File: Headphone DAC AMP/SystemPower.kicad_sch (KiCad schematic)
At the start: 11 parts, among them U6 MCP1727-1802xSN, U7 MCP1727-3302xSN, U9 TPS717XX

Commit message: Swapped to 0603 caps in order to compact design
Planning on a 100x70mm board shape
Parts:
- C44, C45, C46, C47, C48, C49, C61, C62: footprint Capacitor_SMD:C_0805_2012Metric_Pad1.18x1.45mm_HandSolder -> Capacitor_SMD:C_0603_1608Metric_Pad1.08x0.95mm_HandSolder
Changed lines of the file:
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@@
 			)
 		)
-		(property "Footprint" "Capacitor_SMD:C_0805_2012Metric_Pad1.18x1.45mm_HandSolder"
+		(property "Footprint" "Capacitor_SMD:C_0603_1608Metric_Pad1.08x0.95mm_HandSolder"
 			(at 47.9552 41.91 0)
 			(effects
@@
 			)
 		)
-		(property "Footprint" "Capacitor_SMD:C_0805_2012Metric_Pad1.18x1.45mm_HandSolder"
+		(property "Footprint" "Capacitor_SMD:C_0603_1608Metric_Pad1.08x0.95mm_HandSolder"
 			(at 100.0252 39.37 0)
 			(effects
@@
 			)
 		)
-		(property "Footprint" "Capacitor_SMD:C_0805_2012Metric_Pad1.18x1.45mm_HandSolder"
+		(property "Footprint" "Capacitor_SMD:C_0603_1608Metric_Pad1.08x0.95mm_HandSolder"
 			(at 36.5252 41.91 0)
 			(effects
@@
 			)
 		)
-		(property "Footprint" "Capacitor_SMD:C_0805_2012Metric_Pad1.18x1.45mm_HandSolder"
+		(property "Footprint" "Capacitor_SMD:C_0603_1608Metric_Pad1.08x0.95mm_HandSolder"
 			(at 103.8352 104.14 0)
 			(effects
@@
 			)
 		)
-		(property "Footprint" "Capacitor_SMD:C_0805_2012Metric_Pad1.18x1.45mm_HandSolder"
+		(property "Footprint" "Capacitor_SMD:C_0603_1608Metric_Pad1.08x0.95mm_HandSolder"
 			(at 105.1052 160.02 0)
 			(effects
@@
 			)
 		)
-		(property "Footprint" "Capacitor_SMD:C_0805_2012Metric_Pad1.18x1.45mm_HandSolder"
+		(property "Footprint" "Capacitor_SMD:C_0603_1608Metric_Pad1.08x0.95mm_HandSolder"
 			(at 40.3352 106.68 0)
 			(effects
@@
 			)
 		)
-		(property "Footprint" "Capacitor_SMD:C_0805_2012Metric_Pad1.18x1.45mm_HandSolder"
+		(property "Footprint" "Capacitor_SMD:C_0603_1608Metric_Pad1.08x0.95mm_HandSolder"
 			(at 51.7652 106.68 0)
 			(effects
@@
 			)
 		)
-		(property "Footprint" "Capacitor_SMD:C_0805_2012Metric_Pad1.18x1.45mm_HandSolder"
+		(property "Footprint" "Capacitor_SMD:C_0603_1608Metric_Pad1.08x0.95mm_HandSolder"
 			(at 41.6052 161.29 0)
 			(effects

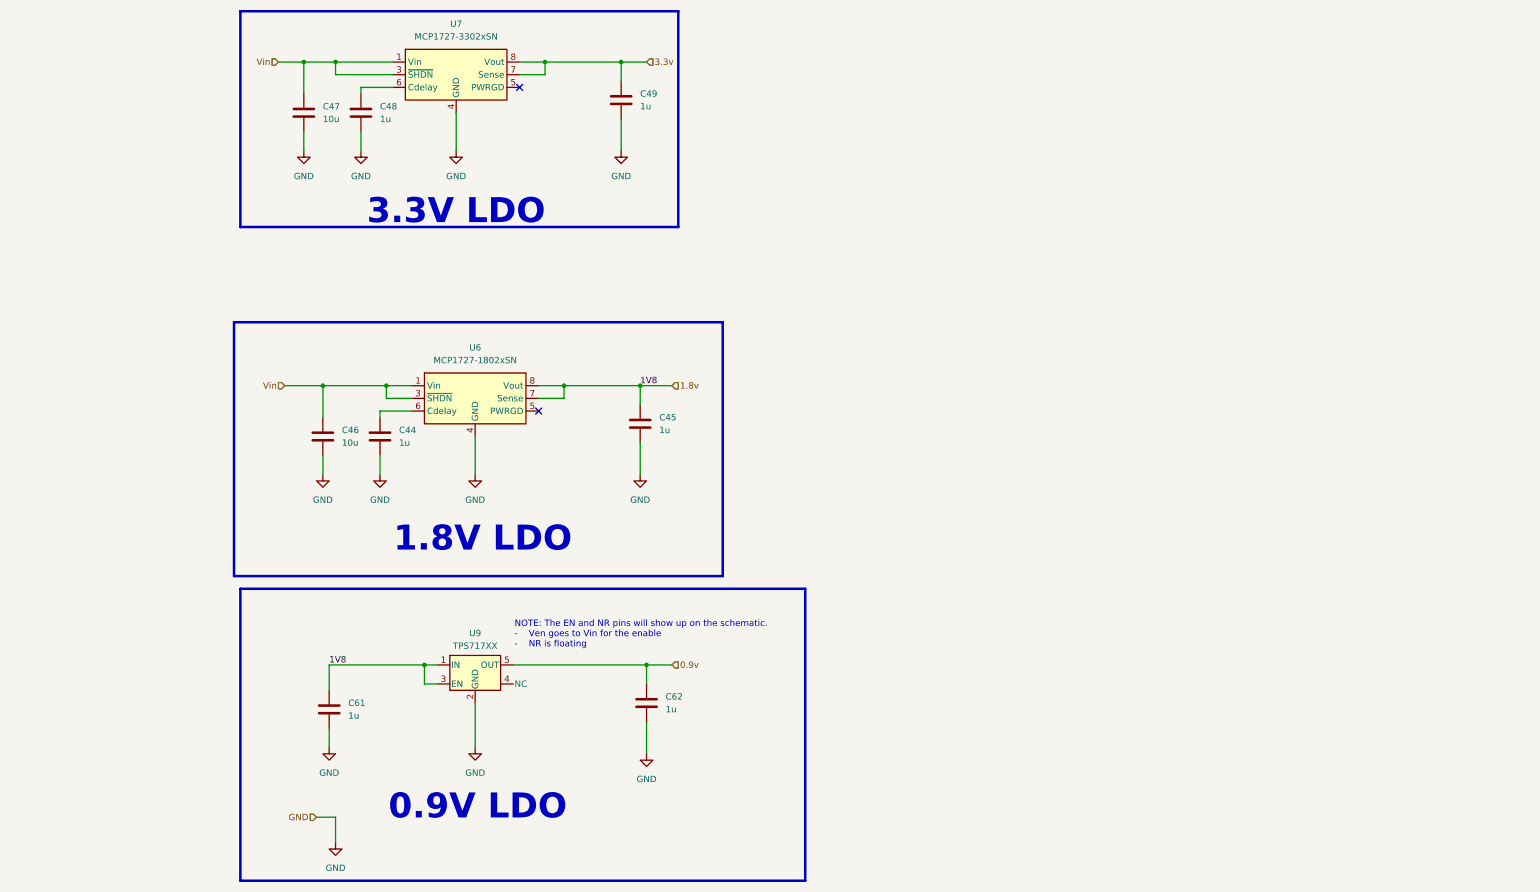
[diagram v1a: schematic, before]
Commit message: (Post Board Order) updated BOM with component links
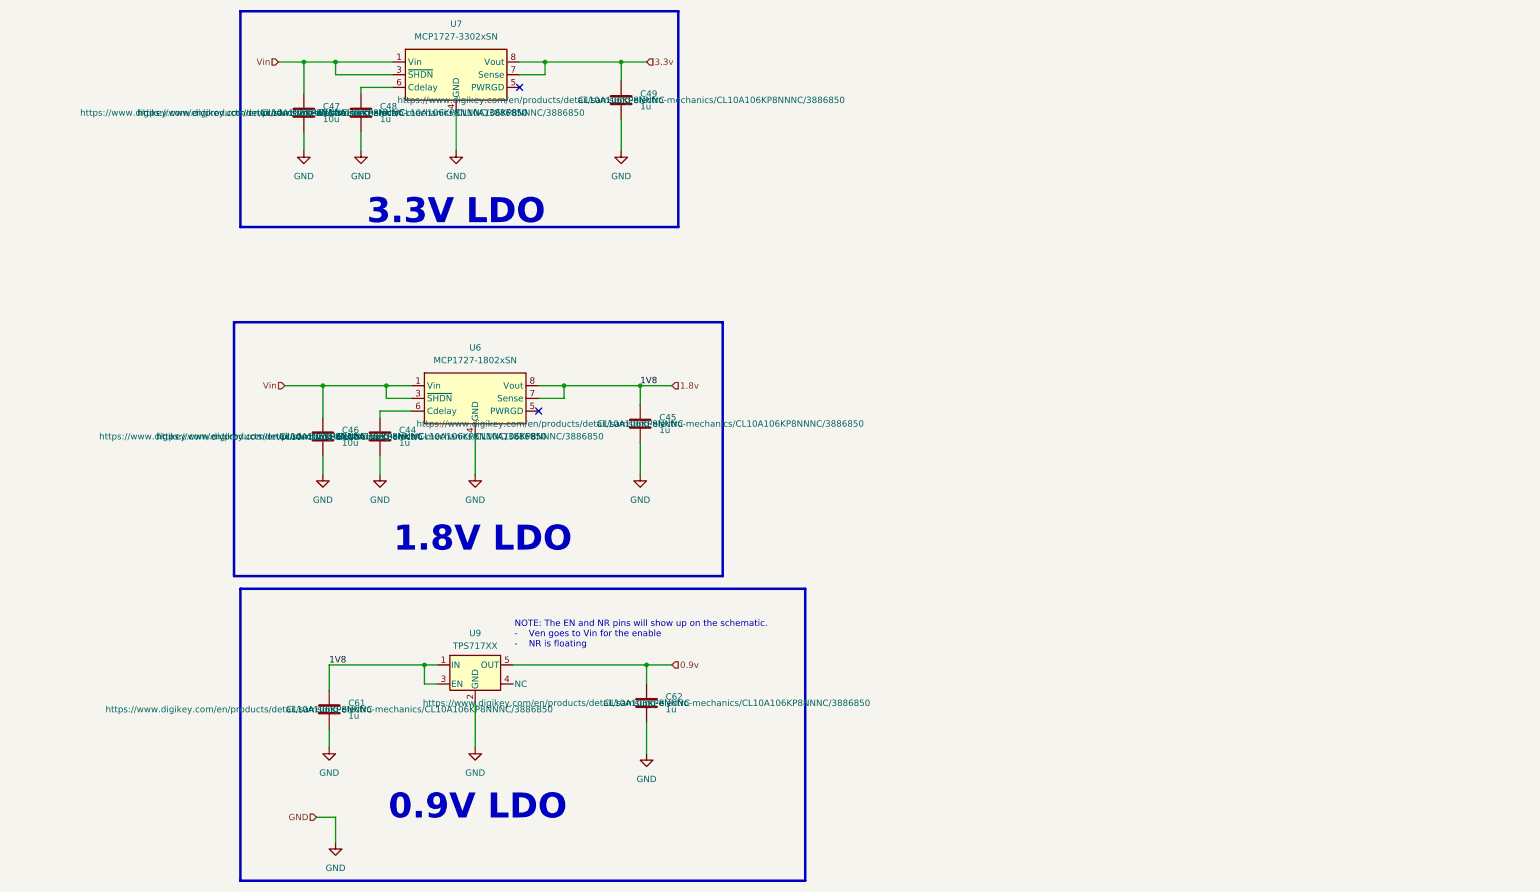
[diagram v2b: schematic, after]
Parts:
- C44, C45, C46, C47, C48, C49, C61, C62: CUI_PURCHASE_URL (none) -> https://www.digikey.com/en/products/detail/samsung-electro-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; Mouser Part Number (none) -> CL10A106KP8NNNC
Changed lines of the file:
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@@
+			)
+		)
+		(property "CUI_PURCHASE_URL" "https://www.digikey.com/en/products/detail/samsung-electro-mechanics/CL10A106KP8NNNC/3886850"
+			(at 46.99 38.1 0)
+			(effects
+				(font
+					(size 1.27 1.27)
+				)
+			)
+		)
+		(property "Mouser Part Number" "CL10A106KP8NNNC"
+			(at 46.99 38.1 0)
+			(effects
+				(font
+					(size 1.27 1.27)
+				)
 			)
 		)
@@
 			)
 		)
+		(property "CUI_PURCHASE_URL" "https://www.digikey.com/en/products/detail/samsung-electro-mechanics/CL10A106KP8NNNC/3886850"
+			(at 99.06 35.56 0)
+			(effects
+				(font
+					(size 1.27 1.27)
+				)
+			)
+		)
+		(property "Mouser Part Number" "CL10A106KP8NNNC"
+			(at 99.06 35.56 0)
+			(effects
+				(font
+					(size 1.27 1.27)
+				)
+			)
+		)
 		(pin "2"
 		)
@@
 			)
 		)
+		(property "CUI_PURCHASE_URL" "https://www.digikey.com/en/products/detail/samsung-electro-mechanics/CL10A106KP8NNNC/3886850"
+			(at 35.56 38.1 0)
+			(effects
+				(font
+					(size 1.27 1.27)
+				)
+			)
+		)
+		(property "Mouser Part Number" "CL10A106KP8NNNC"
+			(at 35.56 38.1 0)
+			(effects
+				(font
+					(size 1.27 1.27)
+				)
+			)
+		)
 		(pin "2"
 		)
@@
 			)
 		)
+		(property "CUI_PURCHASE_URL" "https://www.digikey.com/en/products/detail/samsung-electro-mechanics/CL10A106KP8NNNC/3886850"
+			(at 102.87 100.33 0)
+			(effects
+				(font
+					(size 1.27 1.27)
+				)
+			)
+		)
+		(property "Mouser Part Number" "CL10A106KP8NNNC"
+			(at 102.87 100.33 0)
+			(effects
+				(font
+					(size 1.27 1.27)
+				)
+			)
+		)
 		(pin "2"
 		)
@@
 			)
 		)
+		(property "CUI_PURCHASE_URL" "https://www.digikey.com/en/products/detail/samsung-electro-mechanics/CL10A106KP8NNNC/3886850"
+			(at 104.14 156.21 0)
+			(effects
+				(font
+					(size 1.27 1.27)
+				)
+			)
+		)
+		(property "Mouser Part Number" "CL10A106KP8NNNC"
+			(at 104.14 156.21 0)
+			(effects
+				(font
+					(size 1.27 1.27)
+				)
+			)
+		)
 		(pin "2"
 		)
@@
 			)
 		)
+		(property "CUI_PURCHASE_URL" "https://www.digikey.com/en/products/detail/samsung-electro-mechanics/CL10A106KP8NNNC/3886850"
+			(at 39.37 102.87 0)
+			(effects
+				(font
+					(size 1.27 1.27)
+				)
+			)
+		)
+		(property "Mouser Part Number" "CL10A106KP8NNNC"
+			(at 39.37 102.87 0)
+			(effects
+				(font
+					(size 1.27 1.27)
+				)
+			)
+		)
 		(pin "2"
 		)
@@
 			)
 		)
+		(property "CUI_PURCHASE_URL" "https://www.digikey.com/en/products/detail/samsung-electro-mechanics/CL10A106KP8NNNC/3886850"
+			(at 50.8 102.87 0)
+			(effects
+				(font
+					(size 1.27 1.27)
+				)
+			)
+		)
+		(property "Mouser Part Number" "CL10A106KP8NNNC"
+			(at 50.8 102.87 0)
+			(effects
+				(font
+					(size 1.27 1.27)
+				)
+			)
+		)
 		(pin "1"
 		)
@@
 			)
 		)
+		(property "CUI_PURCHASE_URL" "https://www.digikey.com/en/products/detail/samsung-electro-mechanics/CL10A106KP8NNNC/3886850"
+			(at 40.64 157.48 0)
+			(effects
+				(font
+					(size 1.27 1.27)
+				)
+			)
+		)
+		(property "Mouser Part Number" "CL10A106KP8NNNC"
+			(at 40.64 157.48 0)
+			(effects
+				(font
+					(size 1.27 1.27)
+				)
+			)
+		)

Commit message: Removed DAC Components
Removed all analog components and increased vias to 0.3mm
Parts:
- U9: footprint Package_TO_SOT_SMD:SOT-353_SC-70-5 -> Package_TO_SOT_SMD:SOT-23-5

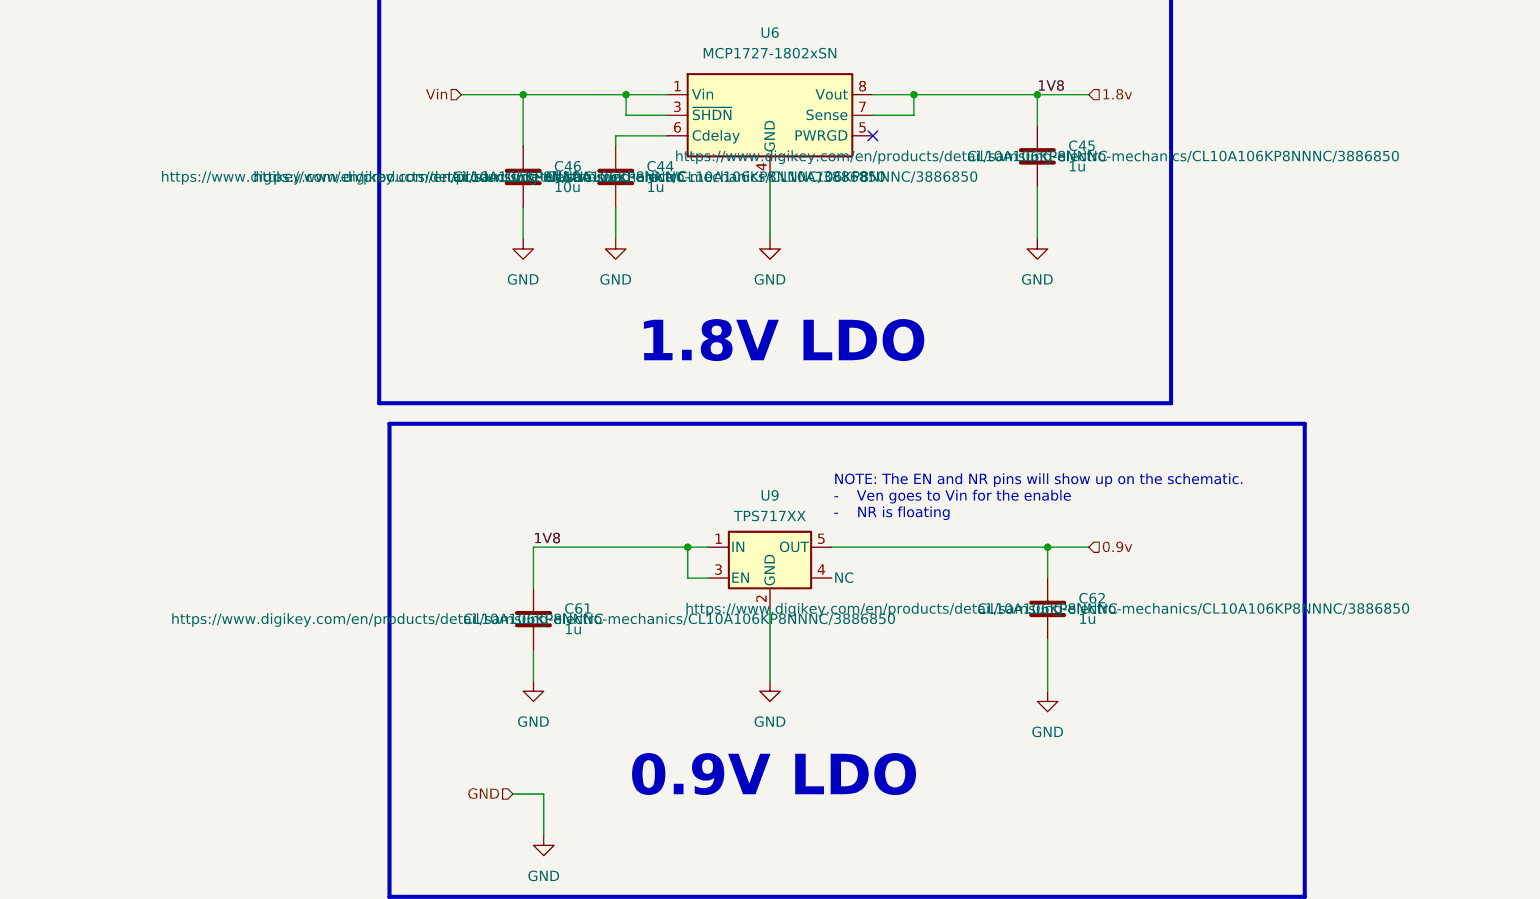
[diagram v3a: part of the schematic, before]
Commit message: Update capacitor footprints
Changed several capacitor footprints in schematic files from 0402/hand-solder variants to standard 0603_1608Metric. Updated PCB with new net and additional property fields for components.
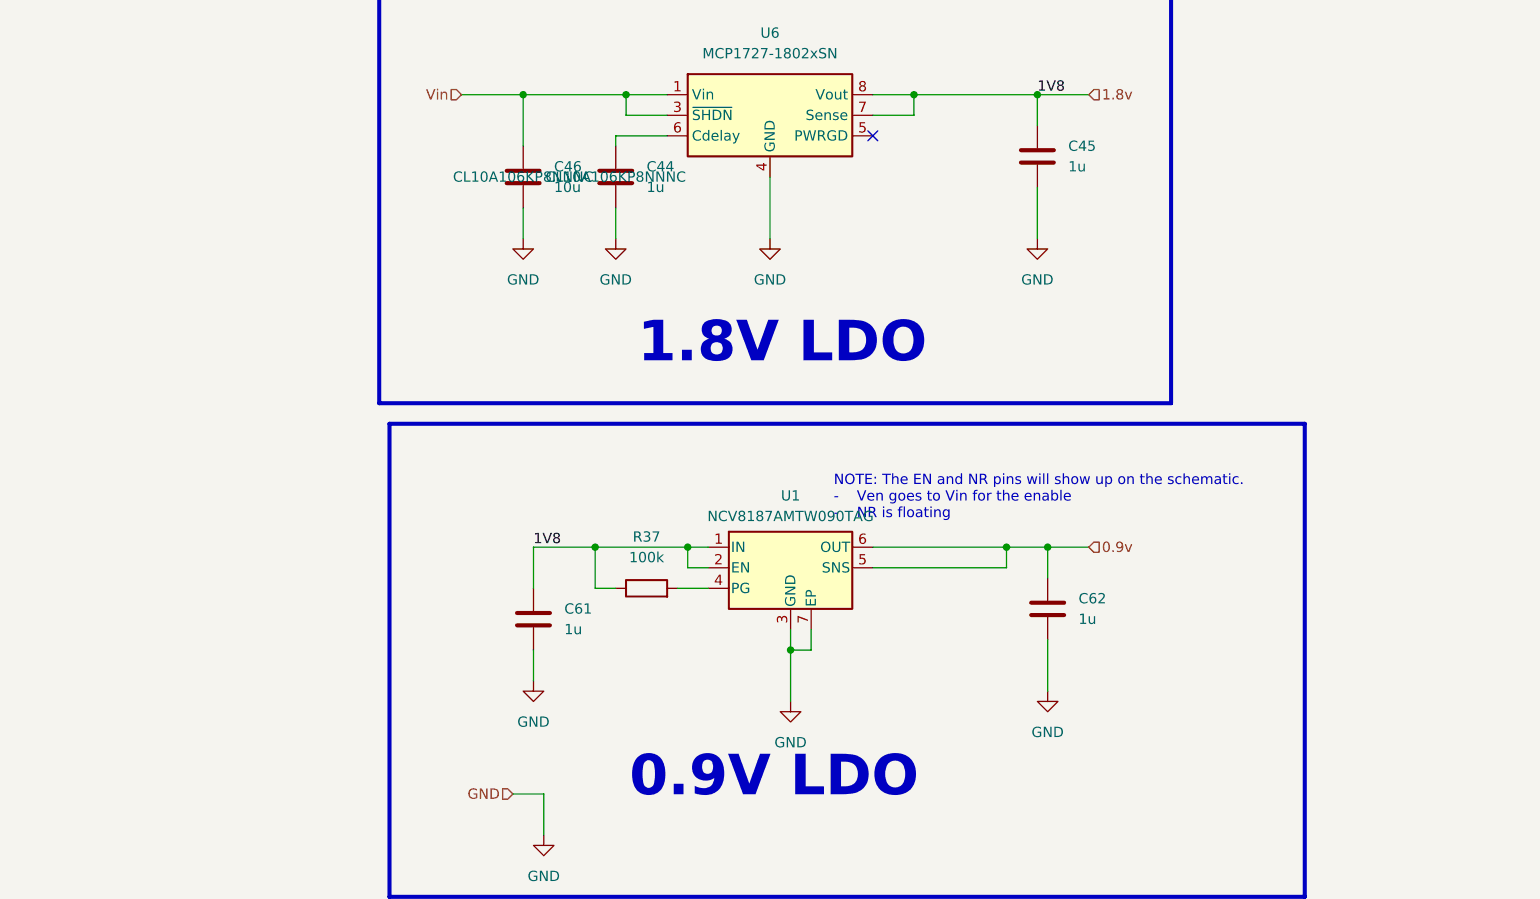
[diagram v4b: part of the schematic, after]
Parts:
- removed U9: TPS717XX, Package_TO_SOT_SMD:SOT-23-5, symbol Regulator_Linear:TPS71518__SC70
- added R37: 100k, Resistor_SMD:R_0805_2012Metric_Pad1.20x1.40mm_HandSolder, symbol Device:R
- added U1: NCV8187AMTW090TAG, Package_SON:WSON-6-1EP_3x3mm_P0.95mm, symbol Regulator_Linear:LP38691SD-5.0
- C44, C45, C46, C47, C48, C49, C61, C62: footprint Capacitor_SMD:C_0603_1608Metric_Pad1.08x0.95mm_HandSolder -> Capacitor_SMD:C_0603_1608Metric
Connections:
- net 0.9v: now also U1.5 (SNS), U1.6 (OUT)
- net 1.8v: now also R37.1, U1.1 (IN), U1.2 (EN), U1.6 (OUT)
- net GND: now also U1.3 (GND), U1.7 (EP)
- new net: R37.2, U1.4 (PG)
